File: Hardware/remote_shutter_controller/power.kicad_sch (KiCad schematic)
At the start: 13 parts

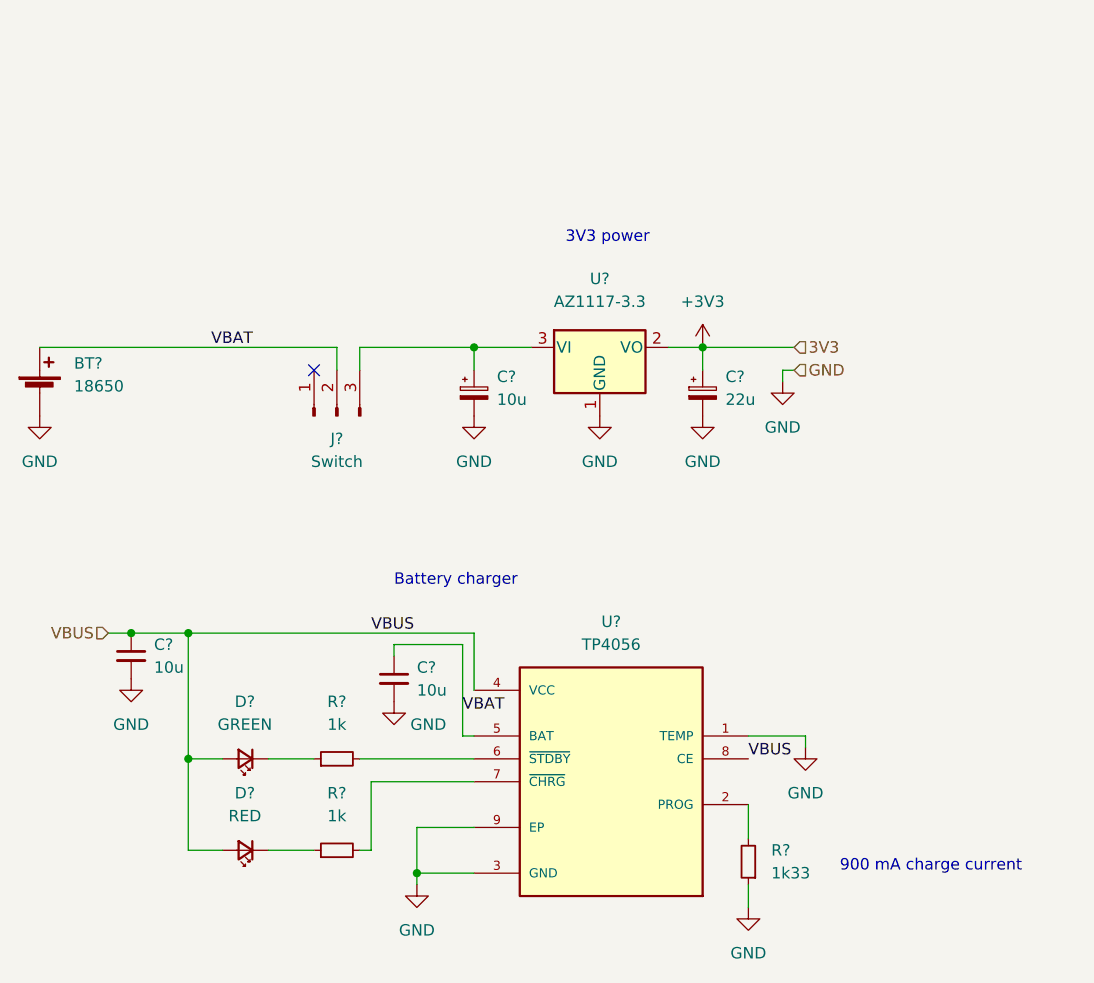
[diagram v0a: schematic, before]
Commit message: Schematic updates. First export to PCB
Added 9V line, OLED switch circuit. Added OLED footprint.
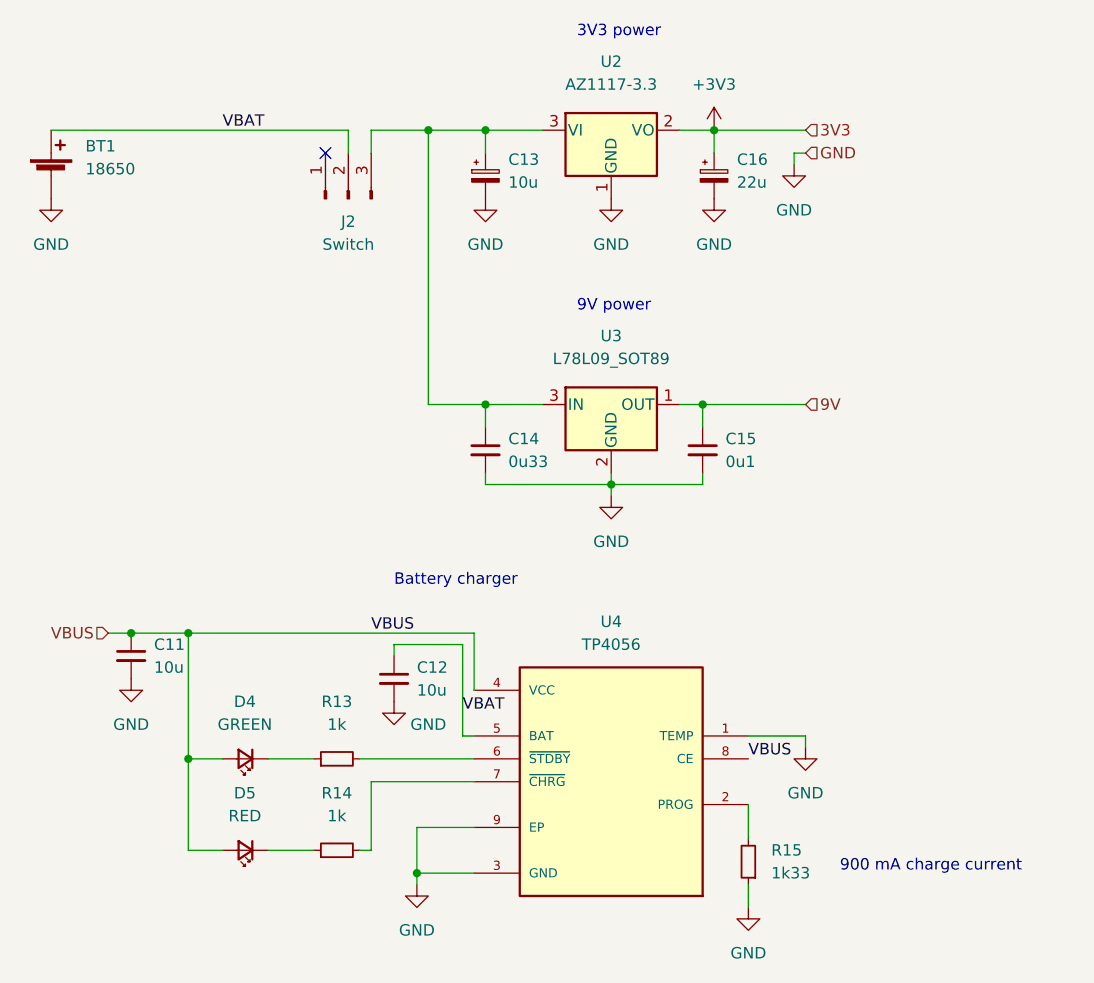
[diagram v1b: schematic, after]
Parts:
- added C14: 0u33, Capacitor_SMD:C_0805_2012Metric_Pad1.18x1.45mm_HandSolder, symbol Device:C_Small
- added C15: 0u1, Capacitor_SMD:C_0805_2012Metric_Pad1.18x1.45mm_HandSolder, symbol Device:C_Small
- added U3: L78L09_SOT89, Package_TO_SOT_SMD:SOT-89-3, symbol Regulator_Linear:L78L09_SOT89
- gave numbers to parts that had none: 13
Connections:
- net GND: now also C14.2, C15.2, U3.2 (GND)
- net at C13.1, J2.3 (Pin_3), U2.3 (VI): now also C14.1, U3.3 (IN)
- new net 9V: C15.1, U3.1 (OUT)
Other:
- note added: "9V power"
- moved on the sheet: BT1, C13, C16, J2, U2

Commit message: Layout pre-routing
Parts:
- BT1: footprint Connector_PinHeader_2.54mm:PinHeader_1x02_P2.54mm_Vertical -> Connector_JST:JST_PH_S2B-PH-K_1x02_P2.00mm_Horizontal
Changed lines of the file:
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@@
       (effects (font (size 1.27 1.27)) (justify left))
     )
-    (property "Footprint" "Connector_PinHeader_2.54mm:PinHeader_1x02_P2.54mm_Vertical" (id 2) (at 95.25 48.006 90)
+    (property "Footprint" "Connector_JST:JST_PH_S2B-PH-K_1x02_P2.00mm_Horizontal" (id 2) (at 95.25 48.006 90)
       (effects (font (size 1.27 1.27)) hide)
     )
